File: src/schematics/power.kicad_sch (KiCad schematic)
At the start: 43 parts, among them U1 L6981NDR, U2 L6981NDR, U3 ST1S41PHR, U4 L6981NDR, U5 LM3880

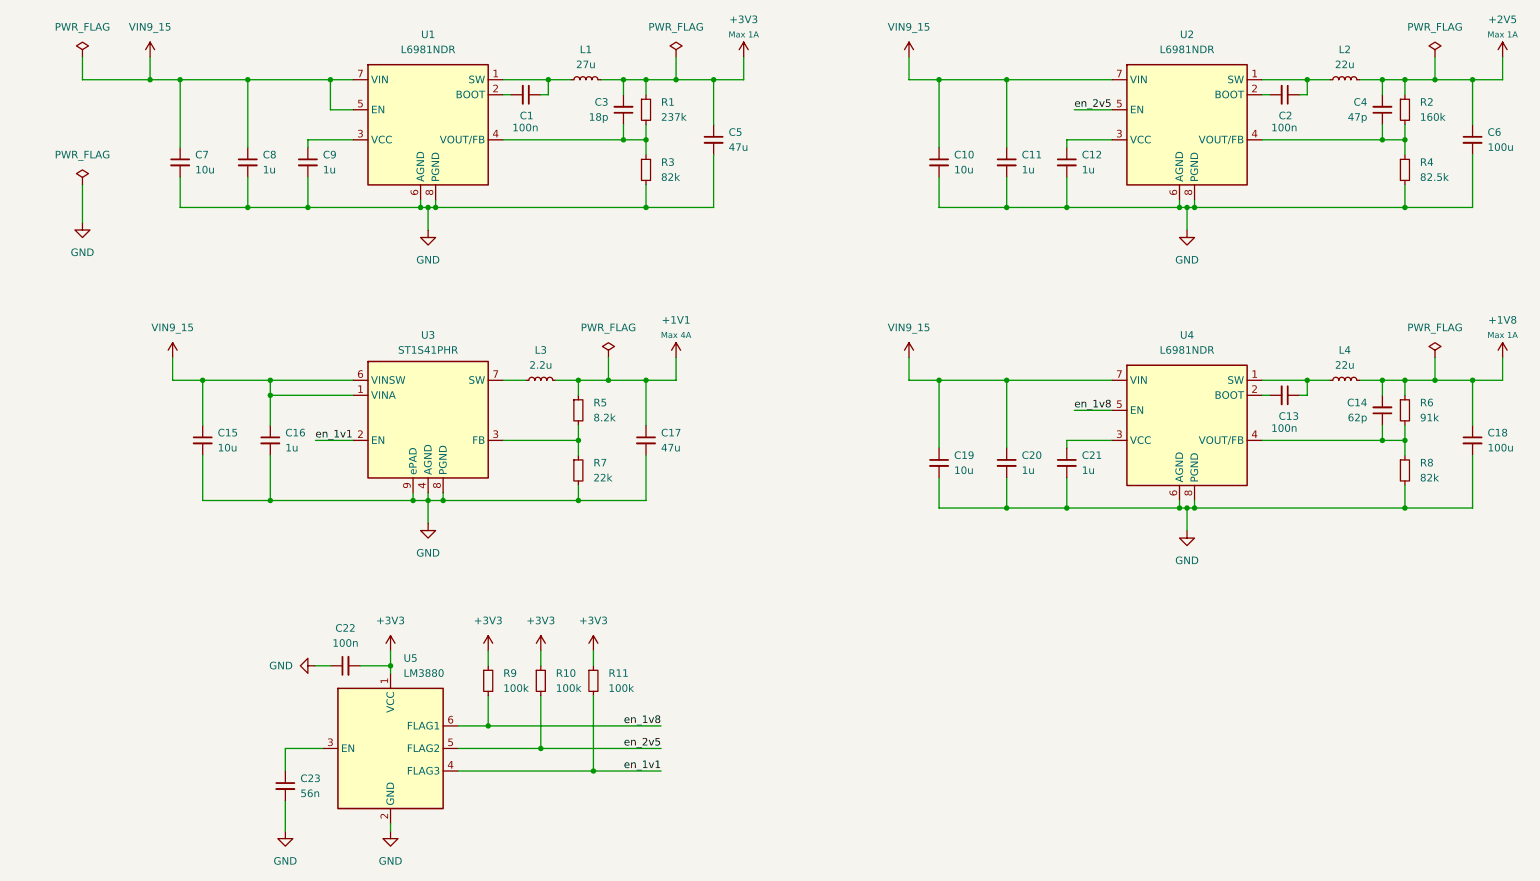
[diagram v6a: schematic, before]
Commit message: Added the reference of passive components from the DC-DC converters (#62)
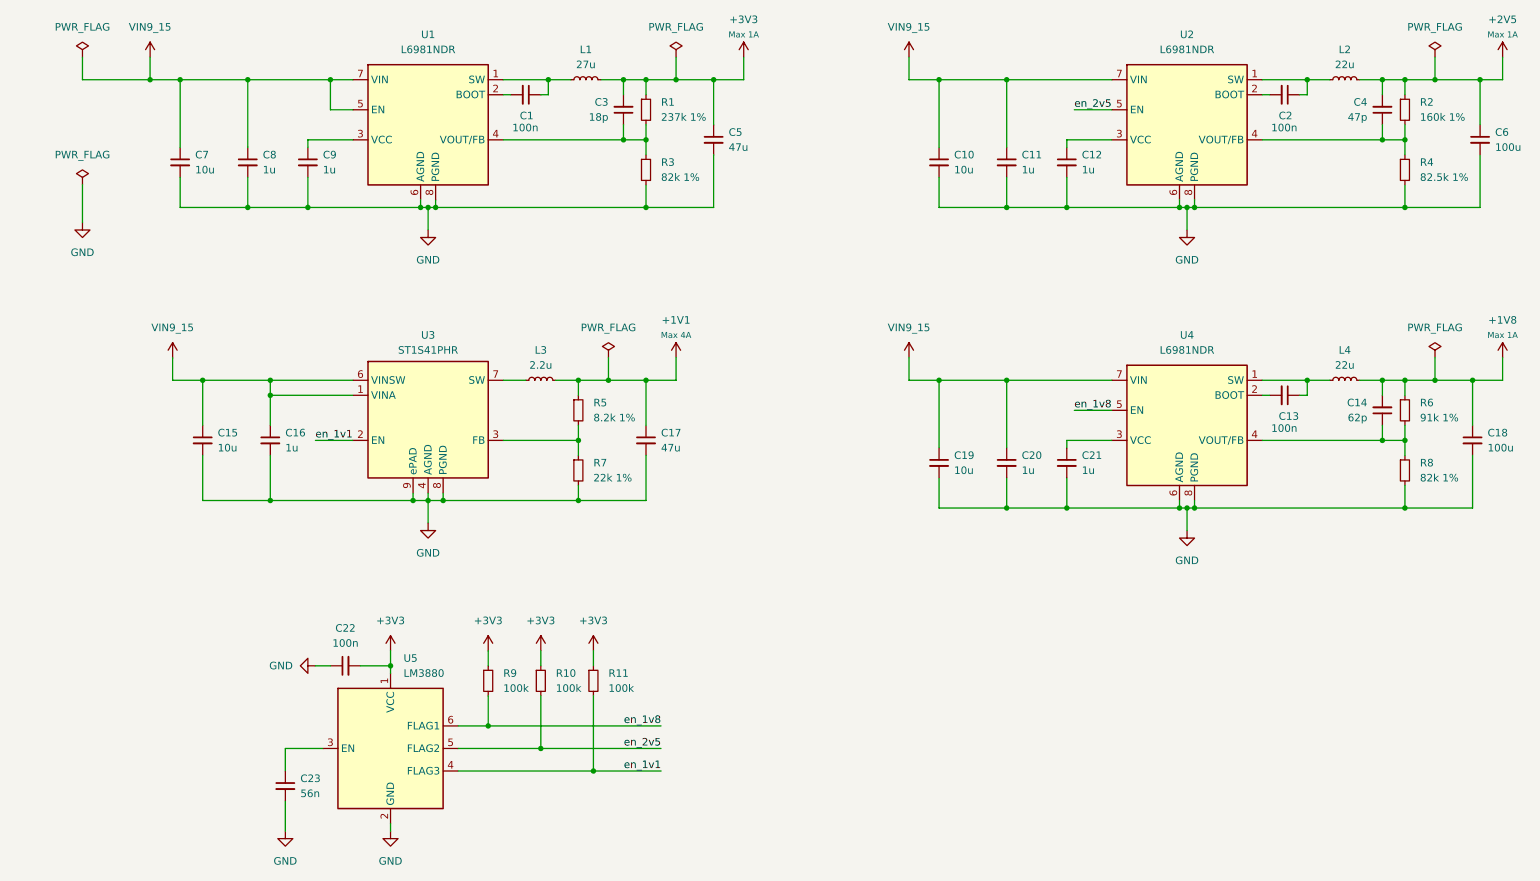
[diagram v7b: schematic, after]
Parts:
- C10, C15, C19, C7: footprint (none) -> Capacitor_SMD:C_1206_3216Metric; Component (none) -> GRM319R61E106KA12D
- C17, C5: footprint (none) -> Capacitor_SMD:C_1210_3225Metric; Component (none) -> 12106D476MAT2A
- C18, C6: footprint (none) -> Capacitor_SMD:C_1210_3225Metric; Component (none) -> GRM32ER60J107ME20L
- L1: Component (none) -> 744770127
- L2, L4: Component (none) -> ETQ-P5M220YFC
- L3: Component (none) -> ETQ-P3M2R2KVP
- R1: value 237k -> 237k 1%
- R2: value 160k -> 160k 1%
- R3, R8: value 82k -> 82k 1%
- R4: value 82.5k -> 82.5k 1%
- R5: value 8.2k -> 8.2k 1%
- R6: value 91k -> 91k 1%
- R7: value 22k -> 22k 1%
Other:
- moved on the sheet: C6
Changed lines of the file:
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@@
 	)
 	(junction
-		(at 261.62 34.29)
-		(diameter 0)
-		(color 0 0 0 0)
-	)
-	(junction
 		(at 213.36 106.68)
 		(diameter 0)
@@
 	)
 	(junction
+		(at 262.89 34.29)
+		(diameter 0)
+		(color 0 0 0 0)
+	)
+	(junction
 		(at 250.19 85.09)
 		(diameter 0)
@@
 	(wire
 		(pts
-			(xy 255.27 34.29) (xy 261.62 34.29)
+			(xy 255.27 34.29) (xy 262.89 34.29)
 		)
 		(stroke
@@
 	(wire
 		(pts
-			(xy 261.62 55.88) (xy 250.19 55.88)
+			(xy 250.19 55.88) (xy 262.89 55.88)
 		)
 		(stroke
@@
 	(wire
 		(pts
-			(xy 266.7 34.29) (xy 261.62 34.29)
+			(xy 266.7 34.29) (xy 262.89 34.29)
 		)
 		(stroke
@@
 	(wire
 		(pts
-			(xy 261.62 41.91) (xy 261.62 34.29)
+			(xy 262.89 41.91) (xy 262.89 34.29)
 		)
 		(stroke
@@
 	(wire
 		(pts
-			(xy 261.62 46.99) (xy 261.62 55.88)
+			(xy 262.89 46.99) (xy 262.89 55.88)
 		)
 		(stroke
@@
 			)
 		)
-		(property "Footprint" ""
+		(property "Footprint" "Capacitor_SMD:C_1206_3216Metric"
 			(at 43.18 48.26 0)
 			(effects
@@
 			)
 		)
+		(property "Component" "GRM319R61E106KA12D"
+			(at 43.18 48.26 0)
+			(effects
+				(font
+					(size 1.27 1.27)
+				)
+				(hide yes)
+			)
+		)
 		(pin "2"
 		)
@@
 		(on_board yes)
 		(dnp no)
-		(fields_autoplaced yes)
 		(property "Reference" "R5"
 			(at 113.03 88.8999 0)
@@
 			)
 		)
-		(property "Value" "8.2k"
+		(property "Value" "8.2k 1%"
 			(at 113.03 91.4399 0)
 			(effects
@@
 			)
 		)
-		(property "Footprint" ""
+		(property "Footprint" "Capacitor_SMD:C_1206_3216Metric"
 			(at 171.45 99.06 0)
 			(effects
@@
 			)
 		)
+		(property "Component" "GRM319R61E106KA12D"
+			(at 171.45 99.06 0)
+			(effects
+				(font
+					(size 1.27 1.27)
+				)
+				(hide yes)
+			)
+		)
 		(pin "2"
 		)
@@
 			)
 		)
-		(property "Value" "91k"
+		(property "Value" "91k 1%"
 			(at 252.73 91.4399 0)
 			(effects
@@
 			)
 		)
-		(property "Value" "22k"
+		(property "Value" "22k 1%"
 			(at 113.03 101.5999 0)
 			(effects
@@
 			)
 		)
-		(property "Footprint" ""
+		(property "Footprint" "Capacitor_SMD:C_1206_3216Metric"
 			(at 171.45 48.26 0)
 			(effects
@@
 			)
 		)
+		(property "Component" "GRM319R61E106KA12D"
+			(at 171.45 48.26 0)
+			(effects
+				(font
+					(size 1.27 1.27)
+				)
+				(hide yes)
+			)
+		)
 		(pin "2"
 		)
@@
 			)
 		)
-		(property "Value" "82.5k"
+		(property "Value" "82.5k 1%"
 			(at 252.73 50.7999 0)
 			(effects
@@
 			)
 		)
+		(property "Component" "744770127"
+			(at 111.76 34.29 90)
+			(effects
+				(font
+					(size 1.27 1.27)
+				)
+				(hide yes)
+			)
+		)
 		(pin "2"
 		)
@@
 			)
 		)
-		(property "Value" "82k"
+		(property "Value" "82k 1%"
 			(at 124.46 50.7999 0)
 			(effects
@@
 			)
 		)
+		(property "Component" "ETQ-P5M220YFC"
+			(at 240.03 34.29 90)
+			(effects
+				(font
+					(size 1.27 1.27)
+				)
+				(hide yes)
+			)
+		)
 		(pin "2"
 		)
@@
 			)
 		)
-		(property "Value" "237k"
+		(property "Value" "237k 1%"
 			(at 124.46 40.6399 0)
 			(effects
@@
 			)
 		)
+		(property "Component" "ETQ-P3M2R2KVP"
+			(at 104.14 85.09 90)
+			(effects
+				(font
+					(size 1.27 1.27)
+				)
+				(hide yes)
+			)
+		)
 		(pin "2"
 		)
@@
 			)
 		)
-		(property "Value" "160k"
+		(property "Value" "160k 1%"
 			(at 252.73 40.6399 0)
 			(effects
@@
 			)
 		)
-		(property "Footprint" ""
+		(property "Footprint" "Capacitor_SMD:C_1210_3225Metric"
 			(at 261.62 95.25 0)
 			(effects
@@
 			)
 		)
+		(property "Component" "GRM32ER60J107ME20L"
+			(at 261.62 95.25 0)
+			(effects
+				(font
+					(size 1.27 1.27)
+				)
+				(hide yes)
+			)
+		)
 		(pin "2"
 		)
@@
 			)
 		)
-		(property "Footprint" ""
+		(property "Footprint" "Capacitor_SMD:C_1210_3225Metric"
 			(at 121.92 95.25 0)
 			(effects
@@
 			)
 		)
+		(property "Component" "12106D476MAT2A"
+			(at 121.92 95.25 0)
+			(effects
+				(font
+					(size 1.27 1.27)
+				)
+				(hide yes)
+			)
+		)
 		(pin "2"
 		)
@@
 	(symbol
 		(lib_id "Device:C_Small")
-		(at 261.62 44.45 0)
+		(at 262.89 44.45 0)
 		(unit 1)
 		(exclude_from_sim no)
@@
 		(fields_autoplaced yes)
 		(property "Reference" "C6"
-			(at 264.16 43.1862 0)
+			(at 265.43 43.1862 0)
 			(effects
 				(font
@@
 		)
 		(property "Value" "100u"
-			(at 264.16 45.7262 0)
+			(at 265.43 45.7262 0)
 			(effects
 				(font
@@
 			)
 		)
-		(property "Footprint" ""
-			(at 261.62 44.45 0)
+		(property "Footprint" "Capacitor_SMD:C_1210_3225Metric"
+			(at 262.89 44.45 0)
 			(effects
 				(font
@@
 		)
 		(property "Datasheet" "~"
-			(at 261.62 44.45 0)
+			(at 262.89 44.45 0)
 			(effects
 				(font
@@
 		)
 		(property "Description" "Unpolarized capacitor, small symbol"
-			(at 261.62 44.45 0)
+			(at 262.89 44.45 0)
+			(effects
+				(font
+					(size 1.27 1.27)
+				)
+				(hide yes)
+			)
+		)
+		(property "Component" "GRM32ER60J107ME20L"
+			(at 262.89 44.45 0)
 			(effects
 				(font
@@
 			)
 		)
-		(property "Footprint" ""
+		(property "Footprint" "Capacitor_SMD:C_1210_3225Metric"
 			(at 133.35 44.45 0)
 			(effects
@@
 			)
 		)
+		(property "Component" "12106D476MAT2A"
+			(at 133.35 44.45 0)
+			(effects
+				(font
+					(size 1.27 1.27)
+				)
+				(hide yes)
+			)
+		)
 		(pin "2"
 		)
@@
 			)
 		)
-		(property "Footprint" ""
+		(property "Footprint" "Capacitor_SMD:C_1206_3216Metric"
 			(at 46.99 95.25 0)
 			(effects
@@
 			)
 		)
+		(property "Component" "GRM319R61E106KA12D"
+			(at 46.99 95.25 0)
+			(effects
+				(font
+					(size 1.27 1.27)
+				)
+				(hide yes)
+			)
+		)
 		(pin "2"
 		)
@@
 			)
 		)
-		(property "Value" "82k"
+		(property "Value" "82k 1%"
 			(at 252.73 101.5999 0)
 			(effects
@@
 			(effects
 				(font
+					(size 1.27 1.27)
+				)
+				(hide yes)
+			)
+		)
+		(property "Component" "ETQ-P5M220YFC"
+			(at 240.03 85.09 90)
+			(effects
+				(font

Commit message: Added footprint for 744770127 (#63)
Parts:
- L1: footprint (none) -> ECAP5-DPROC:744770127
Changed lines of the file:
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@@
 			)
 		)
-		(property "Footprint" ""
+		(property "Footprint" "ECAP5-DPROC:744770127"
 			(at 111.76 34.29 0)
 			(effects
